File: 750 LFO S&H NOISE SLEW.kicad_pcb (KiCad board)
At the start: 2 copper layers, 65 x 106.5 mm, 234 parts, among them J1 JACK_MONO_SW, J10 JACK_MONO_SW, J11 JACK_MONO_SW, J2 JACK_MONO_SW, J3 JACK_MONO_SW, J4 JACK_MONO_SW, J5 JACK_MONO_SW, J6 JACK_MONO_SW, J7 JACK_MONO_SW, J8 JACK_MONO_SW, J9 JACK_MONO_SW, P1 CONN_02X01, P2 CONN_02X01, P3 CONN_02X05, Q1 MMBT3904, Q10 MMBT3904, Q11 J112, Q12 MMBT3906, Q13 J112, Q14 J112, Q15 MMBT3904, Q16 MMBT3904, Q2 MMBT3904, Q3 2N7002, Q4 2N7002, Q5 MBT3946DW, Q6 DMMT3904W, Q7 MMBT3904, Q8 MMBT3904, Q9 MMBT3904, SW1 KS-01Q, SW2 KS-01Q, U1 LM13700, U10 TL072-, U11 TL072-, U12 MAX9945, U13 DG409, U14 DG409, U2 TL072-, U3 TL072-, U4 TL072-, U5 TL072-, U6 CD40106, U7 CD4027, U8 CD4027, U9 TL072-

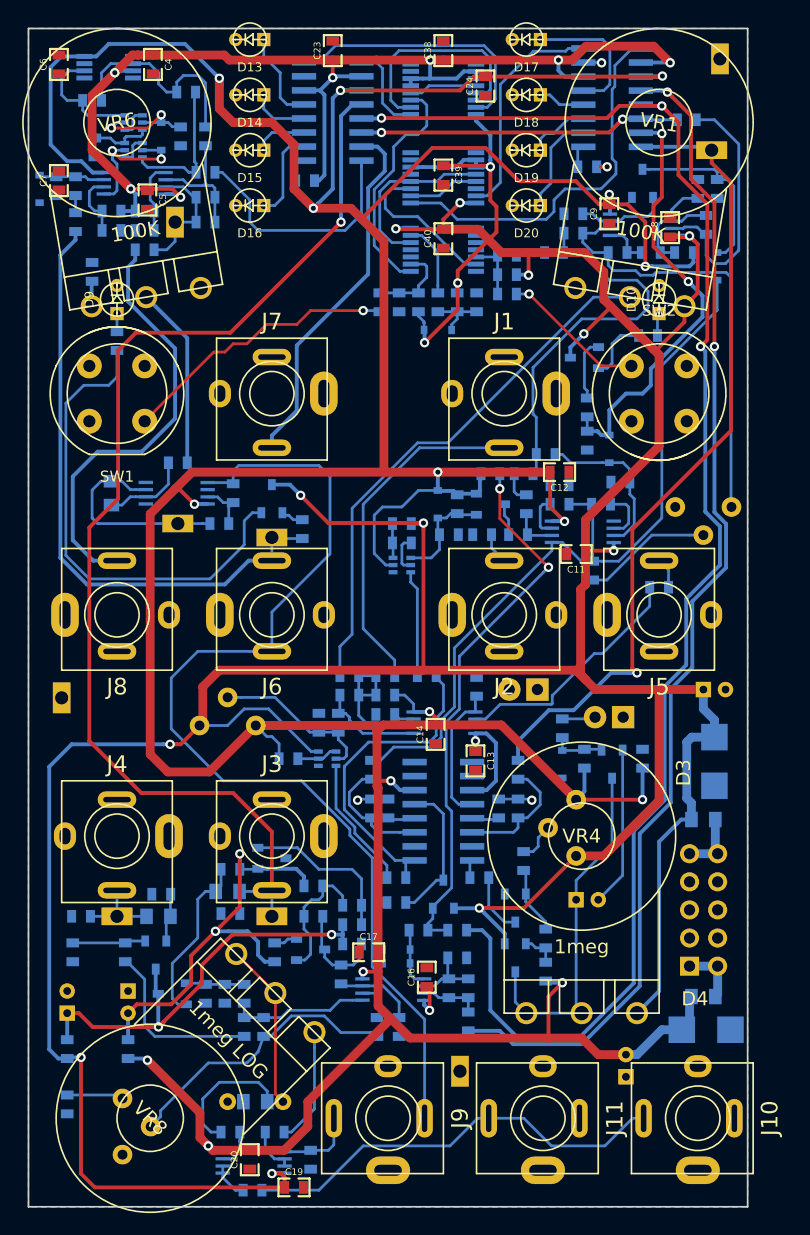
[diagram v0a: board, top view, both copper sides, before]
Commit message: stitching ground plane
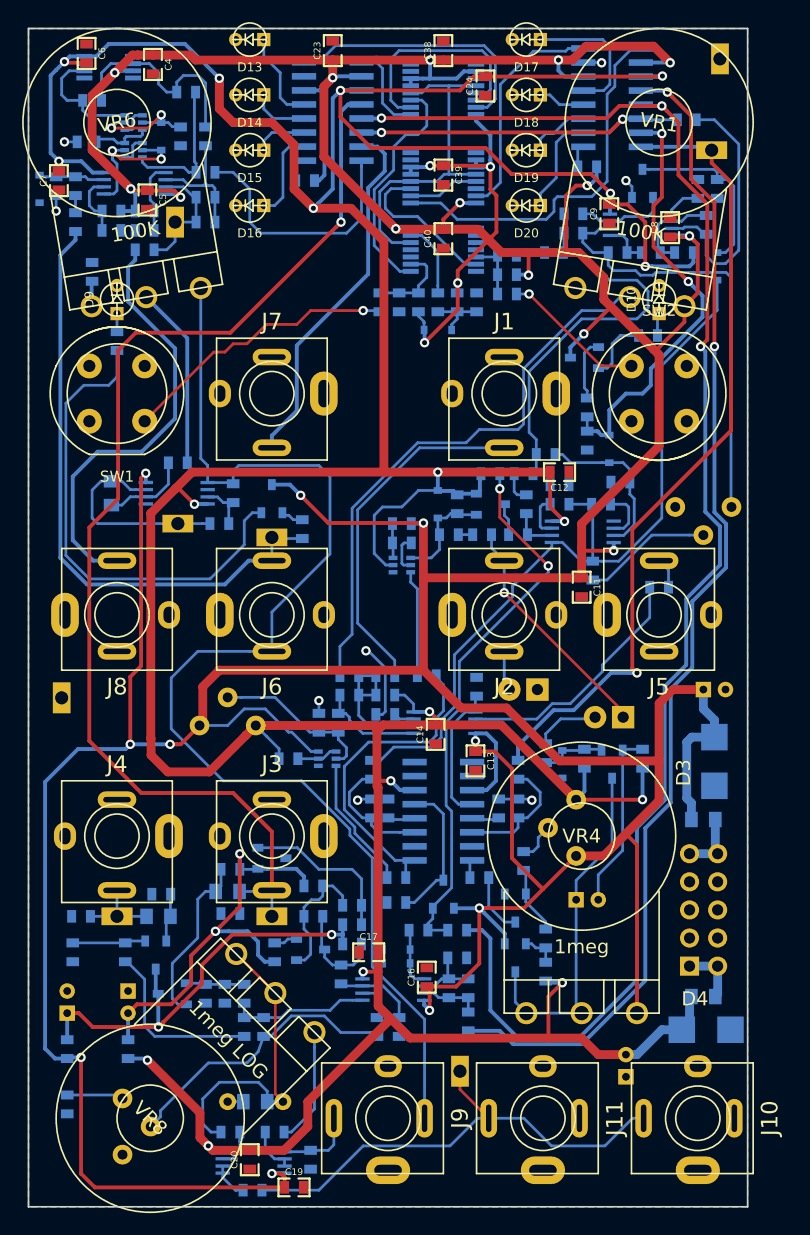
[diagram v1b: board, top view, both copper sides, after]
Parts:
- moved C11 3.04 mm to (110.0, 75.5), turned to 270 degrees
- moved C18 2.70 mm to (106.8, 90.5)
- moved C6 2.69 mm to (65.2, 27.2), turned to 270 degrees
- moved R91 0.90 mm to (65.2, 35.2), turned to 180 degrees
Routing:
- net +12V: track 502.0 -> 579.0 mm, vias 25 -> 28
- net Net-(J2-Pad3): track 2.83 -> 21.4 mm, vias 0 -> 1
- net S&H_INT_CLK: track 94.4 -> 112.2 mm
- net GND: track 7.49 -> 21.7 mm, vias 3 -> 8
- net Net-(U6-Pad12): track 22.3 -> 30.3 mm
- net -12V: track 429.8 -> 435.1 mm, vias 16 -> 18
- net Net-(J10-Pad3): track 39.3 -> 44.6 mm
- net Net-(J2-Pad2): track 0.00 -> 3.64 mm
- net Net-(C18-Pad2): track 3.02 -> 5.98 mm
- net Net-(R4-Pad1): track 48.6 -> 51.5 mm
- net Net-(C27-Pad2): track 14.4 -> 16.3 mm
- net Net-(C44-Pad1): track 27.0 -> 28.5 mm
- net Net-(C15-Pad2): track 0.00 -> 1.30 mm
- net Net-(C18-Pad1): track 4.78 -> 6.01 mm
- net SAMPLE: track 22.0 -> 23.0 mm
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
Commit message: routed
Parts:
- moved C24 0.30 mm to (101.3, 30.5)
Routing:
- net GND: track 21.7 -> 91.2 mm, vias 8 -> 21
- net Net-(U7-Pad13): track 19.6 -> 21.3 mm
- net Net-(U13-Pad16): track 24.2 -> 25.5 mm
- net +12V: track 579.0 -> 580.2 mm
- net LFO_SINE: track 106.9 -> 107.6 mm
- net Net-(U14-Pad16): track 20.4 -> 19.8 mm

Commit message: tidy up
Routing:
- net GND: track 91.2 -> 138.7 mm, vias 21 -> 25
- net PINK_NOISE: track 106.0 -> 102.4 mm
- net Net-(C35-Pad1): track 56.0 -> 56.9 mm
- net Net-(D7-Pad1): track 16.3 -> 15.6 mm
- net Net-(C36-Pad1): track 10.9 -> 10.4 mm

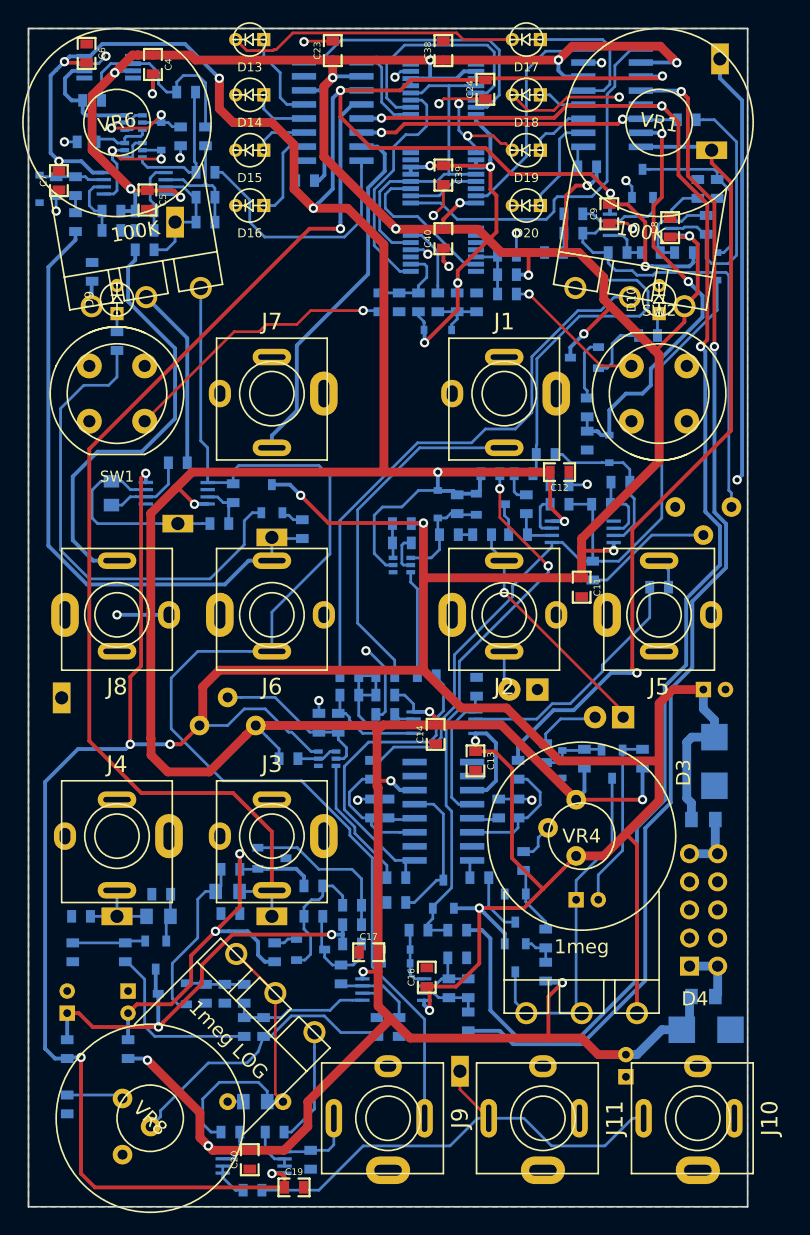
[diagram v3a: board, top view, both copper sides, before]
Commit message: adjust silkscreen
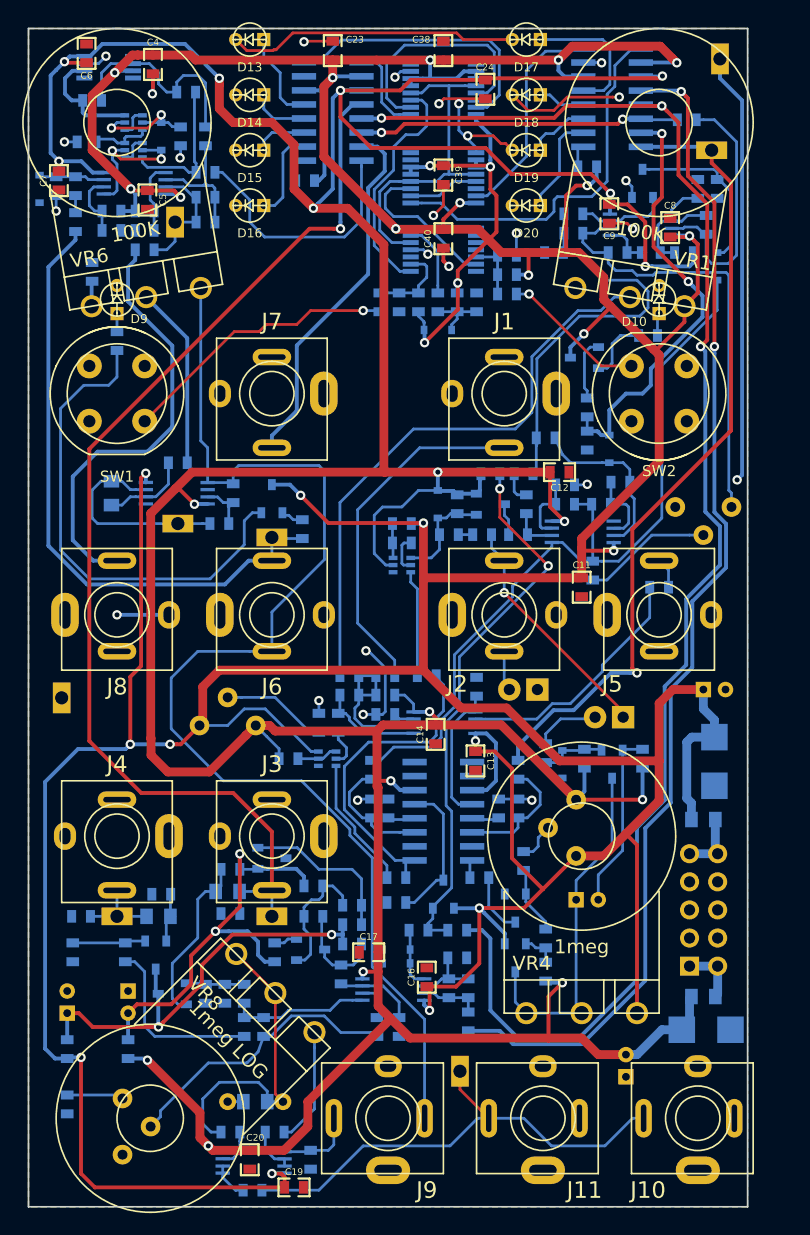
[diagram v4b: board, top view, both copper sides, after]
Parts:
- moved R53 1.50 mm to (106.8, 62.0)
- moved R52 0.50 mm to (108.5, 66.2)
- moved R63 0.50 mm to (108.5, 68.0)
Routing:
- net Net-(R49-Pad2): track 36.2 -> 37.6 mm
- net Net-(D8-Pad1): track 14.7 -> 15.7 mm
- net Net-(R4-Pad1): track 51.6 -> 52.5 mm
- net GND: track 138.7 -> 139.3 mm, vias 25 -> 26
- net Net-(R13-Pad1): track 13.8 -> 14.5 mm
- net Net-(R52-Pad1): track 5.80 -> 6.30 mm
- net Net-(D7-Pad2): track 72.2 -> 71.7 mm
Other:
- board text added: "-12V"
- board text added: "GND"

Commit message: added notes to schematic based on building first prototype
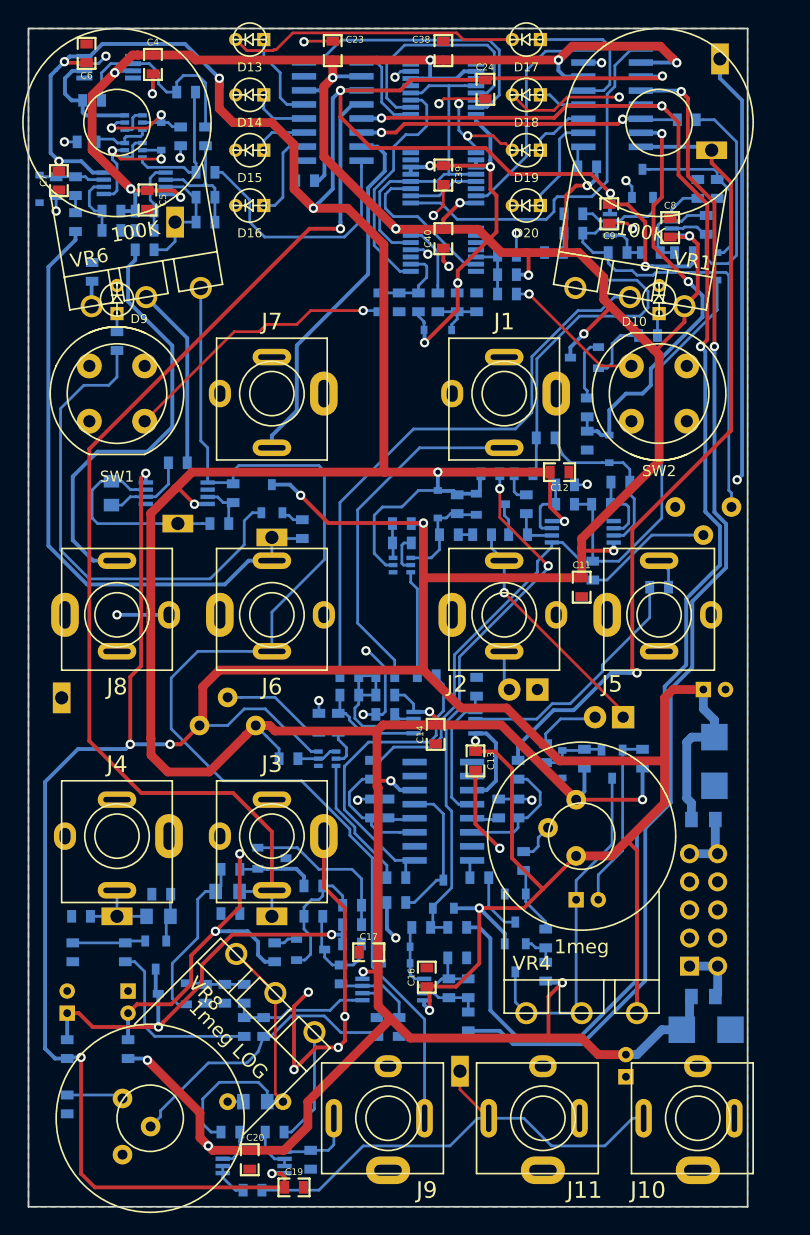
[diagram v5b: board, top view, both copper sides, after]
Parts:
- moved R57 0.35 mm to (95.5, 106.2)
- moved D5 0.25 mm to (93.2, 108.0)
- moved R72 0.25 mm to (98.8, 106.2)
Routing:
- net GND: track 139.3 -> 183.3 mm, vias 26 -> 32
- net Net-(Q13-Pad1): track 53.9 -> 53.4 mm
